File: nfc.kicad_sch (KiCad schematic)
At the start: 0 parts

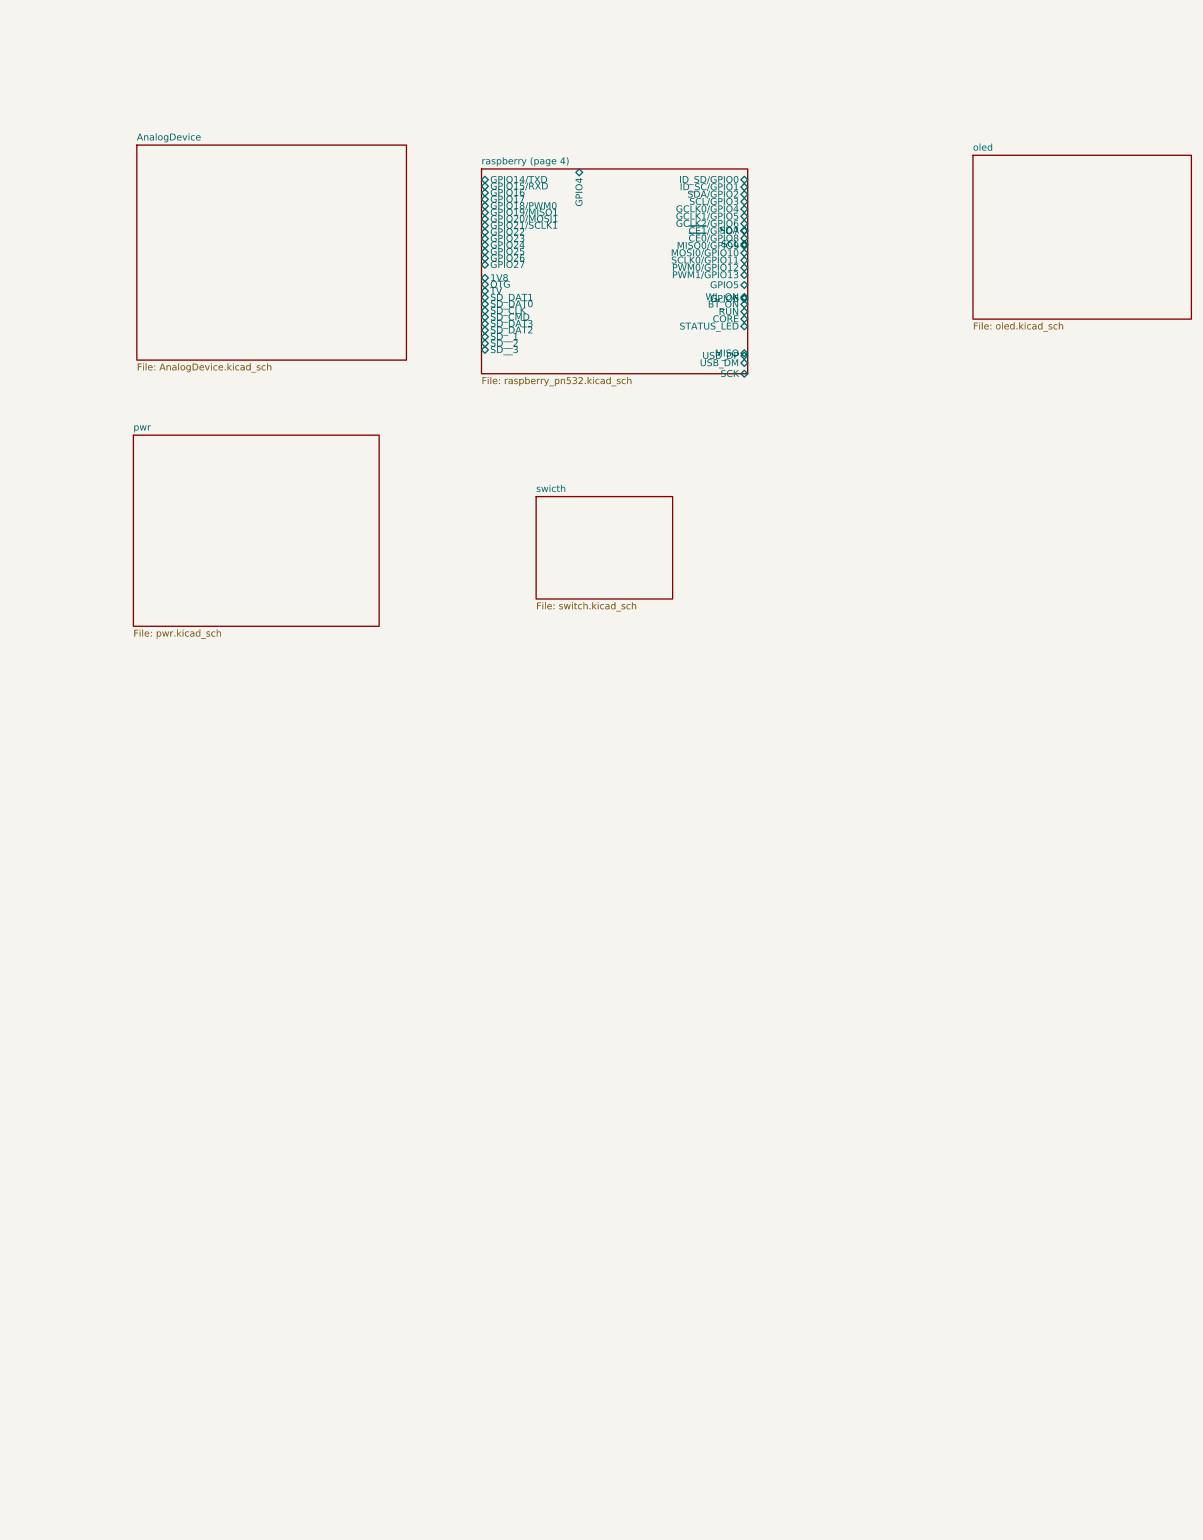
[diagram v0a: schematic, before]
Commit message: Rename sheet to 'Raspberry' and enlarge with 3.5mm pin spacing
- Sheet size: 49.53x115.57 -> 80.0x200.0
- 26 left pins, 27 right pins, 1 top pin
- 3.5mm spacing between hierarchical pins
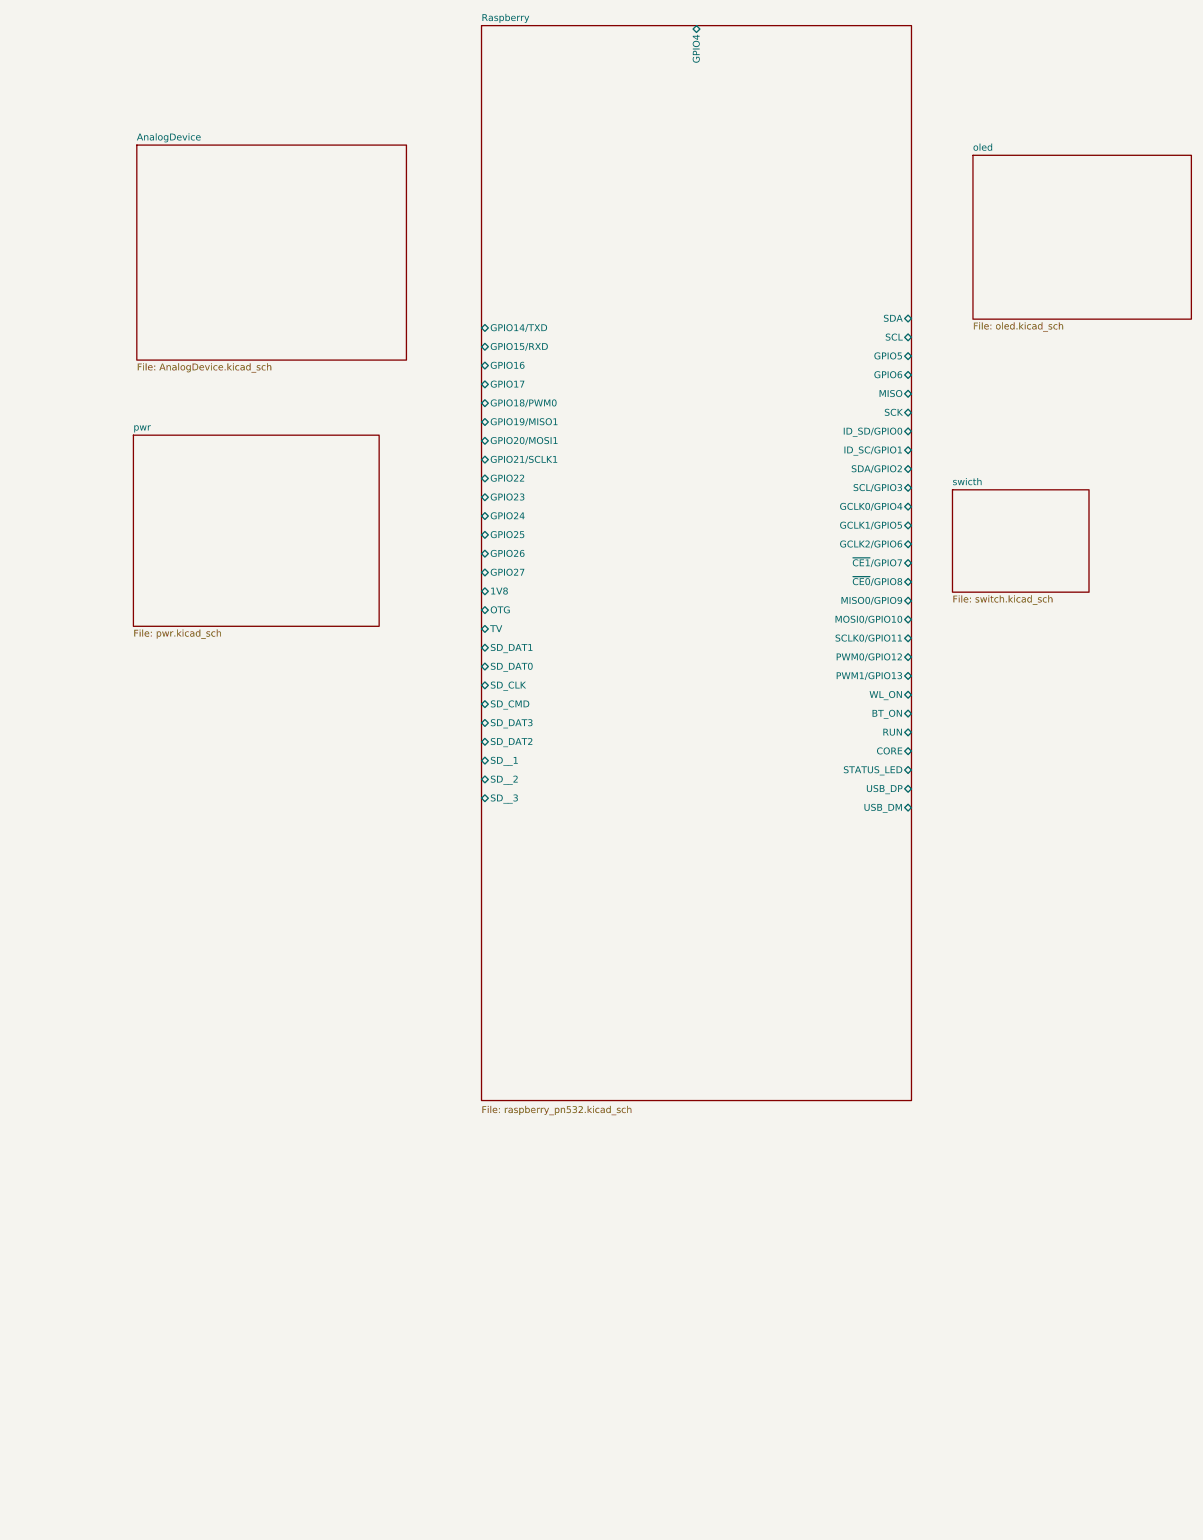
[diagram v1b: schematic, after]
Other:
- sheet raspberry (page 4) renamed Raspberry

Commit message: Rename Raspberry sheet, enlarge to 120x250mm, 5mm pin spacing
- Sheet name: 'raspberry (page 4)' -> 'Raspberry'
- Sheet size: 49.53x38.1 -> 120x250mm
- 26 left pins, 27 right pins with 5mm spacing
- No GND/power pins (removed in prior commits)
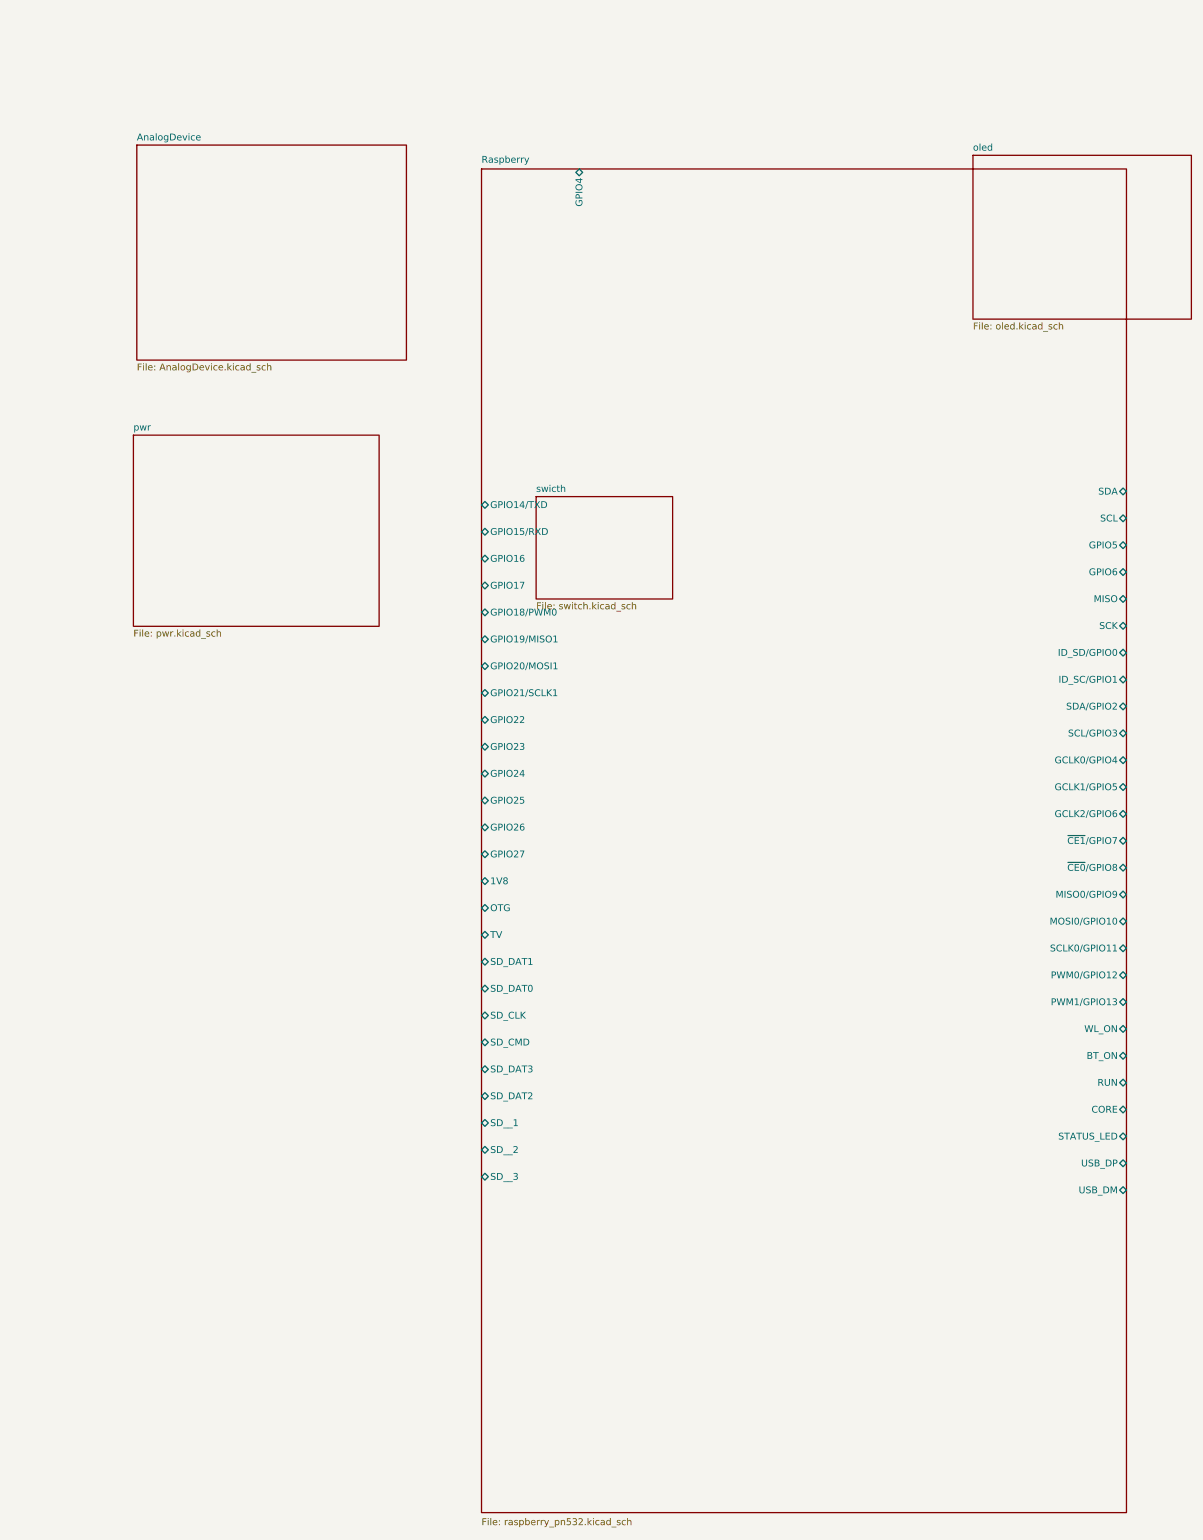
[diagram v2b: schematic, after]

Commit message: Add hierarchical labels/pins across all sheets, fix DiscoveryAnalog3 rename, PCB 99x99mm rounded corners
- nfc_rpi.kicad_sch: 19 hierarchical pins on PN532 sheet
- pn532.kicad_sch: 22 hierarchical labels with _PN532 suffix
- raspberry_pn532.kicad_sch: 68 hierarchical labels for J1
- nfc.kicad_sch: 54 signal pins on Raspberry sheet, power pins removed
- switch.kicad_sch: 8 switch+resistor circuits with hierarchical labels
- oled.kicad_sch: 7 hierarchical labels
- DiscoveryAnalog3.kicad_sch: 26 hierarchical labels for J4 connector
- nfc_rpi.kicad_pcb: 99x99mm board outline with 5mm rounded corners (gr_line + gr_arc)
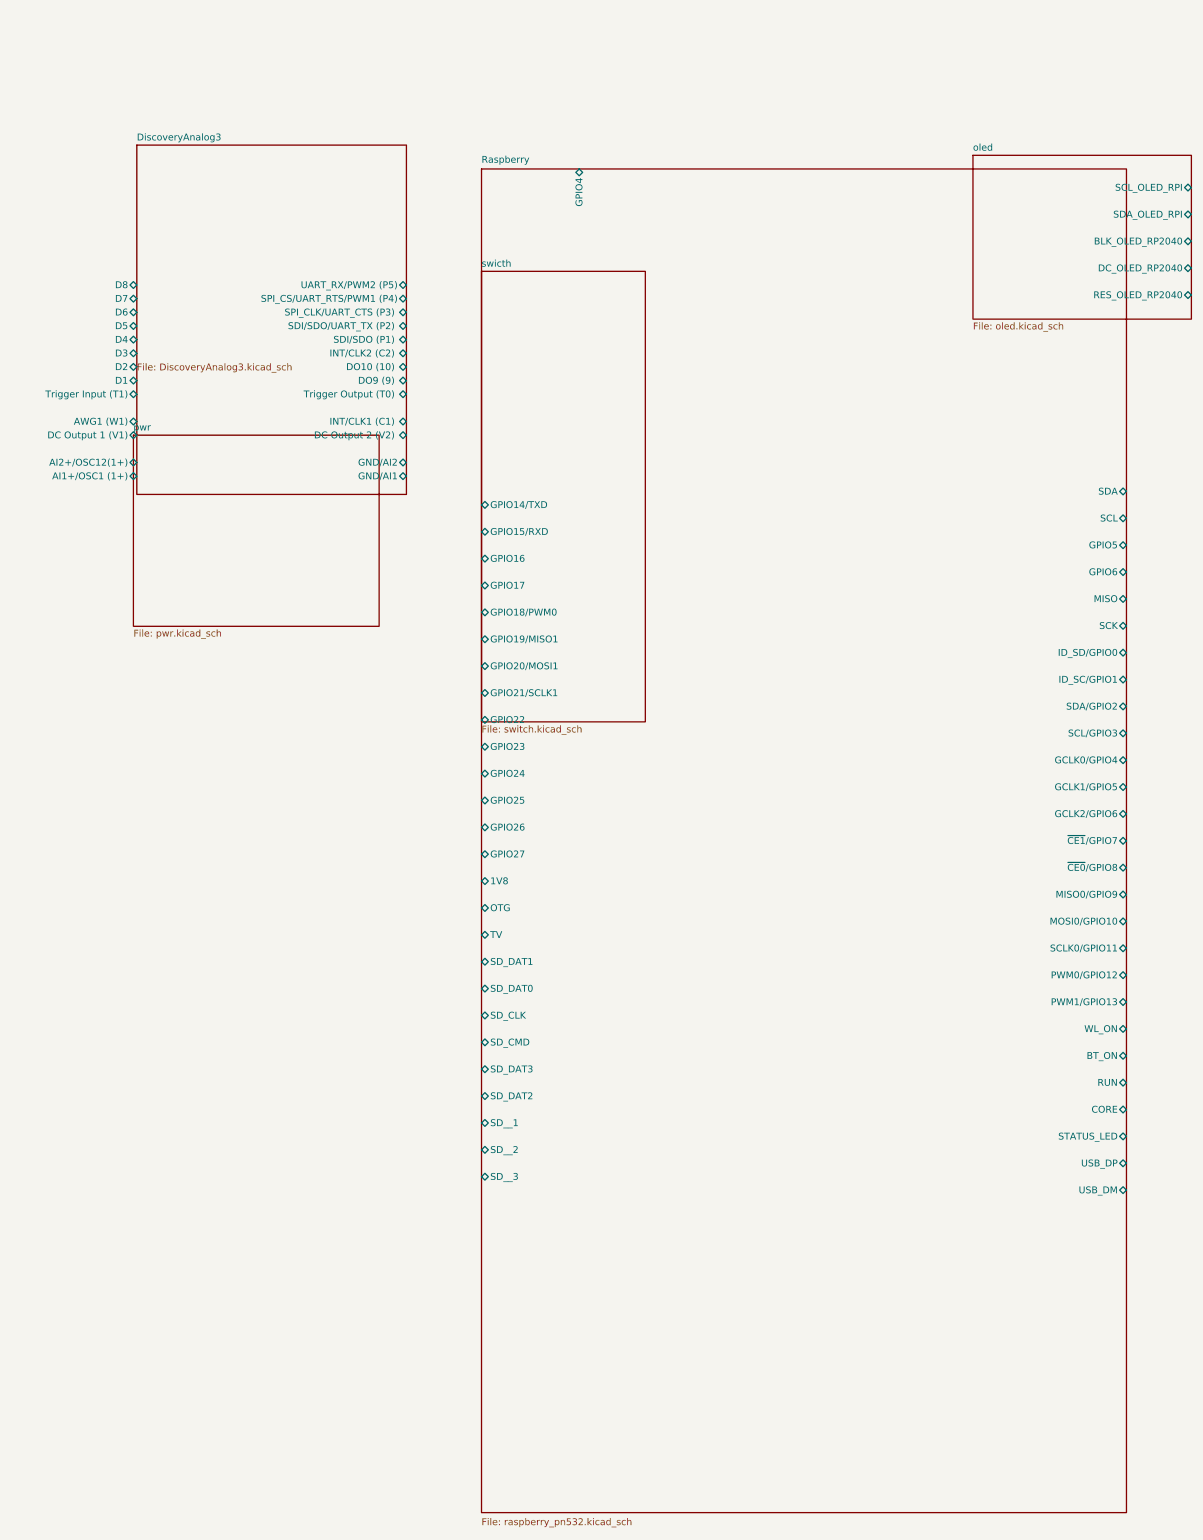
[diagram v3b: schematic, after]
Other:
- sheet AnalogDevice renamed DiscoveryAnalog3
- sheet DiscoveryAnalog3: file AnalogDevice.kicad_sch -> DiscoveryAnalog3.kicad_sch
- sheet DiscoveryAnalog3 ports: added AI1+/OSC1 (1+), AI2+/OSC12(1+), AWG1 (W1), D1, D2, D3, D4, D5, D6, D7, D8, DC Output 1 (V1), DC Output 2 (V2) , DO10 (10) , DO9 (9) , GND/AI1, GND/AI2, INT/CLK1 (C1) , INT/CLK2 (C2) , SDI/SDO (P1) , SDI/SDO/UART_TX (P2) , SPI_CLK/UART_CTS (P3) , SPI_CS/UART_RTS/PWM1 (P4), Trigger Input (T1), Trigger Output (T0) , UART_RX/PWM2 (P5); removed none
- sheet oled ports: added BLK_OLED_RP2040, DC_OLED_RP2040, RES_OLED_RP2040, SCL_OLED_RPI, SDA_OLED_RPI; removed none
